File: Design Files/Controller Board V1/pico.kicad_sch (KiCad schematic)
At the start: 1 part, among them U5 SC0917

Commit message: board
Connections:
- net D_GND is gone; now on net P_GND: U5.13 (GND__2), U5.18 (GND__3), U5.23 (GND__4), U5.28 (GND__5), U5.3 (GND), U5.38 (GND__6), U5.8 (GND__1), U5.D2 (GND__7)
- net PWM_bottom: now also U5.22 (GP17); no longer U5.21 (GP16)
- net PWM_top: now also U5.21 (GP16); no longer U5.22 (GP17)
- net A_GND renamed P_GND
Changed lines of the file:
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@@
+	)
+	(junction
+		(at 161.29 154.94)
+		(diameter 0)
+		(color 0 0 0 0)
 	)
 	(junction
@@
 		)
 	)
-	(hierarchical_label "A_GND"
-		(shape output)
-		(at 158.75 134.62 0)
-		(fields_autoplaced yes)
-		(effects
-			(font
-				(size 1.27 1.27)
-			)
-			(justify left)
-		)
-	)
 	(hierarchical_label "GPIO_5"
 		(shape bidirectional)
@@
 		)
 	)
-	(hierarchical_label "PWM_bottom"
+	(hierarchical_label "PWM_top"
 		(shape output)
 		(at 158.75 76.2 0)
@@
 			)
 			(justify right)
-		)
-	)
-	(hierarchical_label "D_GND"
-		(shape output)
-		(at 161.29 154.94 0)
-		(fields_autoplaced yes)
-		(effects
-			(font
-				(size 1.27 1.27)
-			)
-			(justify left)
 		)
 	)
@@
 		)
 	)
-	(hierarchical_label "PWM_top"
+	(hierarchical_label "PWM_bottom"
 		(shape output)
 		(at 158.75 78.74 0)
@@
 		)
 	)
+	(symbol
+		(lib_id "power:GND")
+		(at 158.75 134.62 90)
+		(unit 1)
+		(exclude_from_sim no)
+		(in_bom yes)
+		(on_board yes)
+		(dnp no)
+		(property "Reference" "#PWR033"
+			(at 165.1 134.62 0)
+			(effects
+				(font
+					(size 1.27 1.27)
+				)
+				(hide yes)
+			)
+		)
+		(property "Value" "P_GND"
+			(at 163.576 134.62 0)
+			(effects
+				(font
+					(size 1.27 1.27)
+				)
+			)
+		)
+		(property "Footprint" ""
+			(at 158.75 134.62 0)
+			(effects
+				(font
+					(size 1.27 1.27)
+				)
+				(hide yes)
+			)
+		)
+		(property "Datasheet" ""
+			(at 158.75 134.62 0)
+			(effects
+				(font
+					(size 1.27 1.27)
+				)
+				(hide yes)
+			)
+		)
+		(property "Description" "Power symbol creates a global label with name \"GND\" , ground"
+			(at 158.75 134.62 0)
+			(effects
+				(font
+					(size 1.27 1.27)
+				)
+				(hide yes)
+			)
+		)
+		(pin "1"
+		)
+		(instances
+			(project "Control Board V1"
+				(path "/e0c606b8-cbb9-4aff-b96c-73876da6ca74/3a200091-b439-443c-a136-2aec626b67e4"
+					(reference "#PWR033")
+					(unit 1)
+				)
+			)
+		)
+	)
+	(symbol
+		(lib_id "power:GND")
+		(at 161.29 154.94 0)
+		(unit 1)
+		(exclude_from_sim no)
+		(in_bom yes)
+		(on_board yes)
+		(dnp no)
+		(property "Reference" "#PWR031"
+			(at 161.29 161.29 0)
+			(effects
+				(font
+					(size 1.27 1.27)
+				)
+				(hide yes)
+			)
+		)
+		(property "Value" "P_GND"
+			(at 161.29 159.766 0)
+			(effects
+				(font
+					(size 1.27 1.27)
+				)
+			)
+		)
+		(property "Footprint" ""
+			(at 161.29 154.94 0)
+			(effects
+				(font
+					(size 1.27 1.27)
+				)
+				(hide yes)
+			)
+		)
+		(property "Datasheet" ""
+			(at 161.29 154.94 0)
+			(effects
+				(font
+					(size 1.27 1.27)
+				)
+				(hide yes)
+			)
+		)
+		(property "Description" "Power symbol creates a global label with name \"GND\" , ground"
+			(at 161.29 154.94 0)
+			(effects
+				(font
+					(size 1.27 1.27)
+				)
+				(hide yes)
+			)
+		)
+		(pin "1"
+		)
+		(instances
+			(project "Control Board V1"
+				(path "/e0c606b8-cbb9-4aff-b96c-73876da6ca74/3a200091-b439-443c-a136-2aec626b67e4"
+					(reference "#PWR031")
+					(unit 1)
+				)
+			)
+		)
+	)

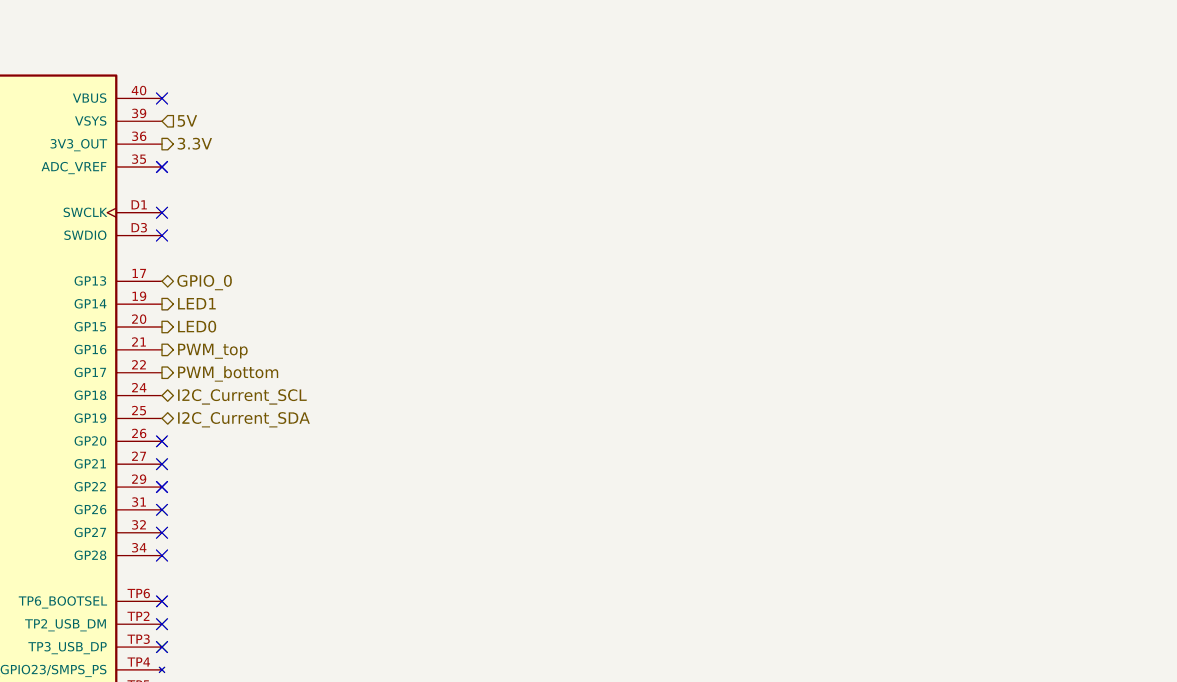
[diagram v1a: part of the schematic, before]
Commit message: Added i2c level shifter
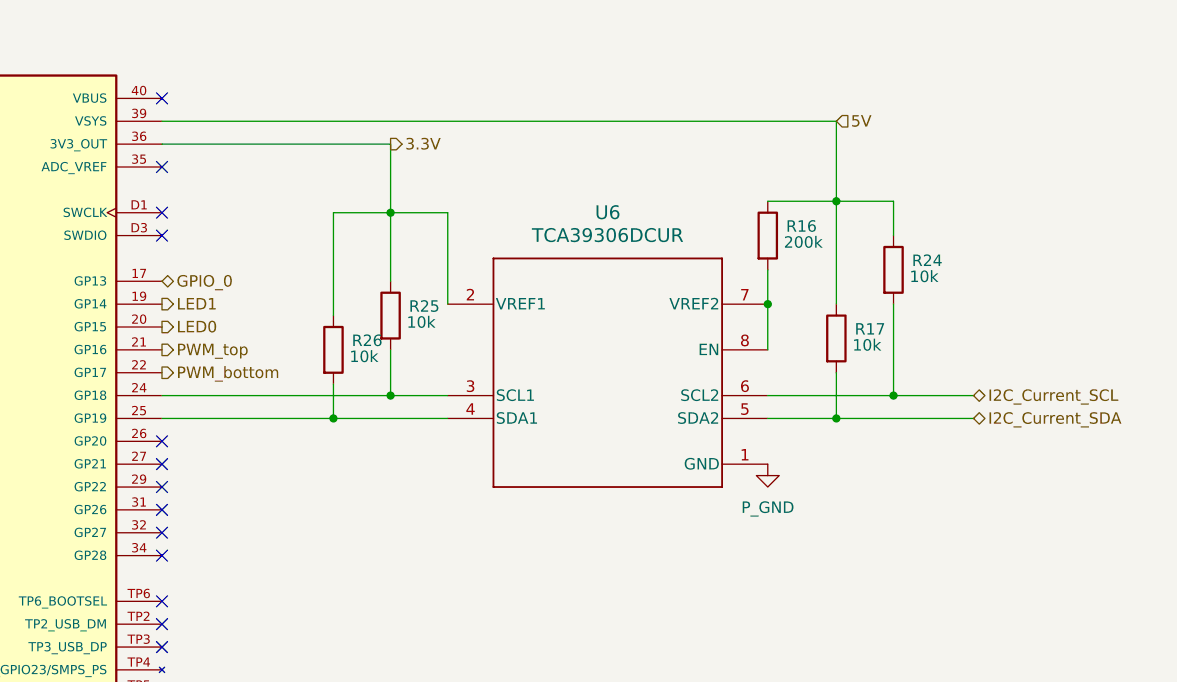
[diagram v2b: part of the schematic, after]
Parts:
- added R16: 200k, PGA460TW:R_0603_1608Metric, symbol Device:R
- added R17, R24, R25, R26: 10k, PGA460TW:R_0603_1608Metric, symbol Device:R
- added U6: TCA39306DCUR, PGA460TW:DCU0008A-MFG, symbol Blaaaaaaaaaaaaaaaaaa:TCA39306DCUR
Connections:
- net 3.3V: now also R25.1, R26.1, U6.2 (VREF1)
- net 5V: now also R16.1, R17.1, R24.1
- net I2C_Current_SCL: now also R24.2, U6.6 (SCL2); no longer U5.24 (GP18)
- net I2C_Current_SDA: now also R17.2, U6.5 (SDA2); no longer U5.25 (GP19)
- net P_GND: now also U6.1 (GND)
- new net: R25.2, U5.24 (GP18), U6.3 (SCL1)
- new net: R26.2, U5.25 (GP19), U6.4 (SDA1)
- new net: R16.2, U6.7 (VREF2), U6.8 (EN)

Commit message: half finished with brooks changes
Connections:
- net P_GND: no longer U5.13 (GND__2), U5.18 (GND__3), U5.23 (GND__4), U5.28 (GND__5), U5.3 (GND), U5.33 (AGND), U5.38 (GND__6), U5.8 (GND__1), U5.D2 (GND__7)
- new net D_GND: U5.13 (GND__2), U5.18 (GND__3), U5.23 (GND__4), U5.28 (GND__5), U5.3 (GND), U5.33 (AGND), U5.38 (GND__6), U5.8 (GND__1), U5.D2 (GND__7)
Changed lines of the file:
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@@
 			)
 		)
-		(property "Value" "P_GND"
+		(property "Value" "D_GND"
 			(at 163.576 134.62 0)
 			(effects
@@
 			)
 		)
-		(property "Value" "P_GND"
+		(property "Value" "D_GND"
 			(at 161.29 159.766 0)
 			(effects

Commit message: i2c stepdown
cookies tmrw
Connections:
- net at R25.2, U6.3 (SCL1): now also U5.25 (GP19); no longer U5.24 (GP18)
- net at R26.2, U6.4 (SDA1): now also U5.24 (GP18); no longer U5.25 (GP19)
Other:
- moved on the sheet: R26
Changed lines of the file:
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@@
-	)
-	(junction
-		(at 177.8 83.82)
-		(diameter 0)
-		(color 0 0 0 0)
 	)
 	(junction
@@
 	)
 	(junction
+		(at 184.15 83.82)
+		(diameter 0)
+		(color 0 0 0 0)
+	)
+	(junction
 		(at 233.68 83.82)
+		(diameter 0)
+		(color 0 0 0 0)
+	)
+	(junction
+		(at 177.8 81.28)
 		(diameter 0)
 		(color 0 0 0 0)
@@
 	)
 	(junction
-		(at 184.15 81.28)
-		(diameter 0)
-		(color 0 0 0 0)
-	)
-	(junction
 		(at 161.29 139.7)
 		(diameter 0)
@@
 	(wire
 		(pts
-			(xy 158.75 83.82) (xy 177.8 83.82)
-		)
-		(stroke
-			(width 0)
-			(type default)
-		)
-	)
-	(wire
-		(pts
 			(xy 158.75 152.4) (xy 161.29 152.4)
 		)
@@
 	(wire
 		(pts
+			(xy 184.15 76.2) (xy 184.15 83.82)
+		)
+		(stroke
+			(width 0)
+			(type default)
+		)
+	)
+	(wire
+		(pts
 			(xy 158.75 50.8) (xy 233.68 50.8)
 		)
@@
 	(wire
 		(pts
+			(xy 177.8 81.28) (xy 190.5 81.28)
+		)
+		(stroke
+			(width 0)
+			(type default)
+		)
+	)
+	(wire
+		(pts
 			(xy 226.06 71.12) (xy 226.06 76.2)
 		)
@@
 	(wire
 		(pts
-			(xy 177.8 60.96) (xy 177.8 72.39)
+			(xy 177.8 60.96) (xy 177.8 68.58)
 		)
 		(stroke
@@
 	(wire
 		(pts
-			(xy 184.15 76.2) (xy 184.15 81.28)
-		)
-		(stroke
-			(width 0)
-			(type default)
-		)
-	)
-	(wire
-		(pts
 			(xy 233.68 50.8) (xy 233.68 59.69)
 		)
@@
 	(wire
 		(pts
-			(xy 184.15 81.28) (xy 190.5 81.28)
-		)
-		(stroke
-			(width 0)
-			(type default)
-		)
-	)
-	(wire
-		(pts
-			(xy 177.8 80.01) (xy 177.8 83.82)
+			(xy 158.75 81.28) (xy 177.8 81.28)
+		)
+		(stroke
+			(width 0)
+			(type default)
+		)
+	)
+	(wire
+		(pts
+			(xy 184.15 83.82) (xy 190.5 83.82)
 		)
 		(stroke
@@
 	(wire
 		(pts
+			(xy 177.8 76.2) (xy 177.8 81.28)
+		)
+		(stroke
+			(width 0)
+			(type default)
+		)
+	)
+	(wire
+		(pts
 			(xy 161.29 147.32) (xy 161.29 149.86)
 		)
@@
 	(wire
 		(pts
-			(xy 177.8 83.82) (xy 190.5 83.82)
+			(xy 158.75 83.82) (xy 184.15 83.82)
 		)
 		(stroke
@@
 		(pts
 			(xy 158.75 149.86) (xy 161.29 149.86)
-		)
-		(stroke
-			(width 0)
-			(type default)
-		)
-	)
-	(wire
-		(pts
-			(xy 158.75 81.28) (xy 184.15 81.28)
 		)
 		(stroke
@@
 		)
 		(instances
-			(project ""
+			(project "Control Board V1"
 				(path "/e0c606b8-cbb9-4aff-b96c-73876da6ca74/3a200091-b439-443c-a136-2aec626b67e4"
 					(reference "U6")
@@
 	(symbol
 		(lib_id "Device:R")
-		(at 177.8 76.2 0)
+		(at 177.8 72.39 0)
 		(unit 1)
 		(exclude_from_sim no)
@@
 		(dnp no)
 		(property "Reference" "R26"
-			(at 179.832 75.184 0)
+			(at 179.832 71.374 0)
 			(effects
 				(font
@@
 		)
 		(property "Value" "10k"
-			(at 179.578 76.962 0)
+			(at 179.578 73.152 0)
 			(effects
 				(font
@@
 		)
 		(property "Footprint" "PGA460TW:R_0603_1608Metric"
-			(at 176.022 76.2 90)
+			(at 176.022 72.39 90)
 			(effects
 				(font
@@
 		)
 		(property "Datasheet" "~"
-			(at 177.8 76.2 0)
+			(at 177.8 72.39 0)
 			(effects
 				(font
@@
 		)
 		(property "Description" "Resistor"
-			(at 177.8 76.2 0)
-			(effects
-				(font
+			(at 177.8 72.39 0)
+			(effects
+				(font

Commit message: Last second changes
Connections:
- net P_GND is gone; now on net D_GND: U6.1 (GND)
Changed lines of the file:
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@@
 		(shape bidirectional)
 		(at 107.95 81.28 180)
-		(fields_autoplaced yes)
 		(effects
 			(font
@@
 		(shape bidirectional)
 		(at 107.95 91.44 180)
-		(fields_autoplaced yes)
 		(effects
 			(font
@@
 		(shape bidirectional)
 		(at 107.95 78.74 180)
-		(fields_autoplaced yes)
 		(effects
 			(font
@@
 		(shape output)
 		(at 158.75 76.2 0)
-		(fields_autoplaced yes)
 		(effects
 			(font
@@
 		(shape output)
 		(at 107.95 83.82 180)
-		(fields_autoplaced yes)
 		(effects
 			(font
@@
 		(shape output)
 		(at 107.95 73.66 180)
-		(fields_autoplaced yes)
 		(effects
 			(font
@@
 		(shape output)
 		(at 107.95 93.98 180)
-		(fields_autoplaced yes)
 		(effects
 			(font
@@
 		(shape output)
 		(at 158.75 73.66 0)
-		(fields_autoplaced yes)
 		(effects
 			(font
@@
 		(shape output)
 		(at 184.15 53.34 0)
-		(fields_autoplaced yes)
 		(effects
 			(font
@@
 		(shape bidirectional)
 		(at 107.95 68.58 180)
-		(fields_autoplaced yes)
 		(effects
 			(font
@@
 		(shape bidirectional)
 		(at 158.75 68.58 0)
-		(fields_autoplaced yes)
 		(effects
 			(font
@@
 		(shape bidirectional)
 		(at 248.92 81.28 0)
-		(fields_autoplaced yes)
 		(effects
 			(font
@@
 		(shape bidirectional)
 		(at 107.95 88.9 180)
-		(fields_autoplaced yes)
 		(effects
 			(font
@@
 		(shape bidirectional)
 		(at 107.95 71.12 180)
-		(fields_autoplaced yes)
 		(effects
 			(font
@@
 		(shape input)
 		(at 233.68 50.8 0)
-		(fields_autoplaced yes)
 		(effects
 			(font
@@
 		(shape output)
 		(at 107.95 86.36 180)
-		(fields_autoplaced yes)
 		(effects
 			(font
@@
 		(shape bidirectional)
 		(at 248.92 83.82 0)
-		(fields_autoplaced yes)
 		(effects
 			(font
@@
 		(shape bidirectional)
 		(at 107.95 99.06 180)
-		(fields_autoplaced yes)
 		(effects
 			(font
@@
 		(shape output)
 		(at 107.95 76.2 180)
-		(fields_autoplaced yes)
 		(effects
 			(font
@@
 		(shape output)
 		(at 158.75 78.74 0)
-		(fields_autoplaced yes)
 		(effects
 			(font
@@
 		(shape output)
 		(at 158.75 71.12 0)
-		(fields_autoplaced yes)
 		(effects
 			(font
@@
 		(shape output)
 		(at 107.95 96.52 180)
-		(fields_autoplaced yes)
 		(effects
 			(font
@@
 			)
 		)
-		(property "Value" "P_GND"
+		(property "Value" "D_GND"
 			(at 226.06 93.726 0)
 			(effects
